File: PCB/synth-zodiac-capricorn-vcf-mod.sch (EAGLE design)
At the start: 35 parts, among them Q10 PNP, Q11 NPN, Q9 PNP, U11 TL074A, U12 LM13700

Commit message: Snapshot of designs so far.
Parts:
- removed C36, C39, C40: 0.1uF, rlc:CAPACITOR0603
- removed CP_GND, CP_LFO_CV: PADSMD-070X070, con-testpoints:PADSMD-070X070
- removed GLYPH1: Virgo, circuit-monkey-zodiac:GLYPH-VIRGO
- removed LED: BLU, led:SMT0603
- removed LFO_SQ, LFO_TRI: TPSMD-040-RND, con-testpoints:TPSMD-040-RND
- removed OUT_VCF, OUT_VCO: 2-pin, VT, SMT, con-jst:02PVT-SMT
- removed PWR: (no value), con-jst:04P-VT-SMT
- removed Q10, Q9: PNP, transistor-bjt:PNP-BC856
- removed Q11: NPN, transistor-bjt:NPN-BC846
- removed R58: 274K, rlc:RESISTOR0603
- removed R59: 3.32, rlc:RESISTOR0603
- removed R60: 221K, rlc:RESISTOR0603
- removed R61, R64: 499K, rlc:RESISTOR0603
- removed R62, R63, R68: 10.0K, rlc:RESISTOR0603
- removed R65: 47.5K, rlc:RESISTOR0603
- removed R66: 1.0K, rlc:RESISTOR0603
- removed R67: 22.1K, rlc:RESISTOR0603
- removed R69: 12.1K, rlc:RESISTOR0603
- removed RATE: 10K, rlc:TRIMPOT9MM_PCB_SHAFT
- removed U11: TL074A, op-amp:QUADTL074A-SOIC
- removed U12: LM13700, op-amp:DUAL-BIASLM13700-SMD
- removed WAVE: SPDT, switch-thd:SLIDE-SPDTSS-12-F45-TH-PCB
- added AMT: 10K, rlc:TRIMPOT9MM_PCB_SHAFT
- added EG, LFO, VCF_OUT: 2-pin, VT, SMT, con-jst:02PVT-SMT
- added J4: (no value), con-jst:04P-VT-SMT
- added POL, SRC: SPDT, switch-thd:SLIDE-SPDTSS-12-F45-TH-PCB
- added R72, R73: 10.0K, rlc:RESISTOR0603
- added U1: TL072A, op-amp:DUALTL072A
- CONST1: value Virgo -> Capricorn; device circuit-monkey-zodiac:CONSTELLATION-VIRGO -> circuit-monkey-zodiac:CONSTELLATION-CAPRICORN
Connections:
- removed net LFO_CV_IN: CP_LFO_CV.PAD, R60.1
- removed net LFO_OSC: R63.2, U11-D.+, U12-A.+, U12-B.+, U12-B.OUT
- removed net LFO_SQ: LFO_SQ.P$1, U11-D.-, U11-D.OUT, WAVE-SW.B
- removed net LFO_TRI: LFO_TRI.P$1, U11-A.-, U11-A.OUT, WAVE-SW.A
- removed net N$76: R58.1, RATE.2
- removed net N$77: Q9.BASE, R58.2, R59.1, R60.2
- removed net N$79: Q9.EMITTER, R61.2, U11-C.+
- removed net N$80: Q10.EMITTER, U11-C.-, U11-C.OUT
- removed net N$81: Q10.COLLECTOR, R62.1
- removed net N$82: R62.2, U12-A.AMP-BIAS
- removed net N$83: C36.1, U12-A-BUFFER.IN, U12-A.OUT
- removed net N$85: R64.1, U11-A.+, U12-A-BUFFER.OUT, U12-B.-
- removed net N$87: R65.1, U12-B.AMP-BIAS
- removed net N$88: Q11.BASE, R67.2, R68.2
- removed net N$89: Q11.EMITTER, R66.1
- removed net N$90: R68.1, R69.1, U12-B-BUFFER.OUT
- removed net N$91: LED.C, Q11.COLLECTOR
- new net AMT: AMT.2, U1-A.+
- new net EG: EG.1, SRC-SW.B
- new net MOD_N: POL-SW.A, R72.2, U1-B.OUT
- new net MOD_P: POL-SW.B, R73.1, U1-A.-, U1-A.OUT
- new net MOD_SRC: AMT.3, SRC-SW.C
- new net N$99: R72.1, R73.2, U1-B.-
- new net VCF_MOD: POL-SW.C, VCF_OUT.1
- net +9V: now also J4.1, U1-PWR.V+; no longer C39.1, LED.A, PWR.1, R61.1, R65.2, R67.1, RATE.3, U11-PWR.V+, U12-PWR.V+
- net -9V: now also J4.2, U1-PWR.V-; no longer C40.2, PWR.2, R64.2, R69.2, RATE.1, U11-PWR.V-, U12-PWR.V-
- net GND: now also AMT.1, EG.2, J4.4, LFO.2, POL-MTG.MT1, POL-MTG.MT2, SRC-MTG.MT1, SRC-MTG.MT2, U1-B.+, VCF_OUT.2; no longer C36.2, C39.2, C40.1, CP_GND.PAD, OUT_VCF.2, OUT_VCO.2, PWR.4, Q10.BASE, Q9.COLLECTOR, R59.2, R63.1, R66.2, U12-A.-
- net LFO_CV: now also LFO.1, SRC-SW.A; no longer OUT_VCF.1, OUT_VCO.1, U12-B-BUFFER.IN, WAVE-SW.C
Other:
- note added: "NC"
- note added: "POLARITY"
- note added: "VCF MODULATOR"
- note added: "VCF Modulation Amount"
- note added: "VCF Modulation Source"
- note added: "[+]"
- note added: "[-]"
- note removed: "==> VCF MOD"
- note removed: "==> VCO MOD"
- note removed: "CV_PNL ===>"
- note removed: "LFO"
- note removed: "LFO RATE"
- note removed: "LFO WAVE"
- note removed: "SQ"
- note removed: "TRI"
- moved on the sheet: C41, C42, CONST1, PCB1

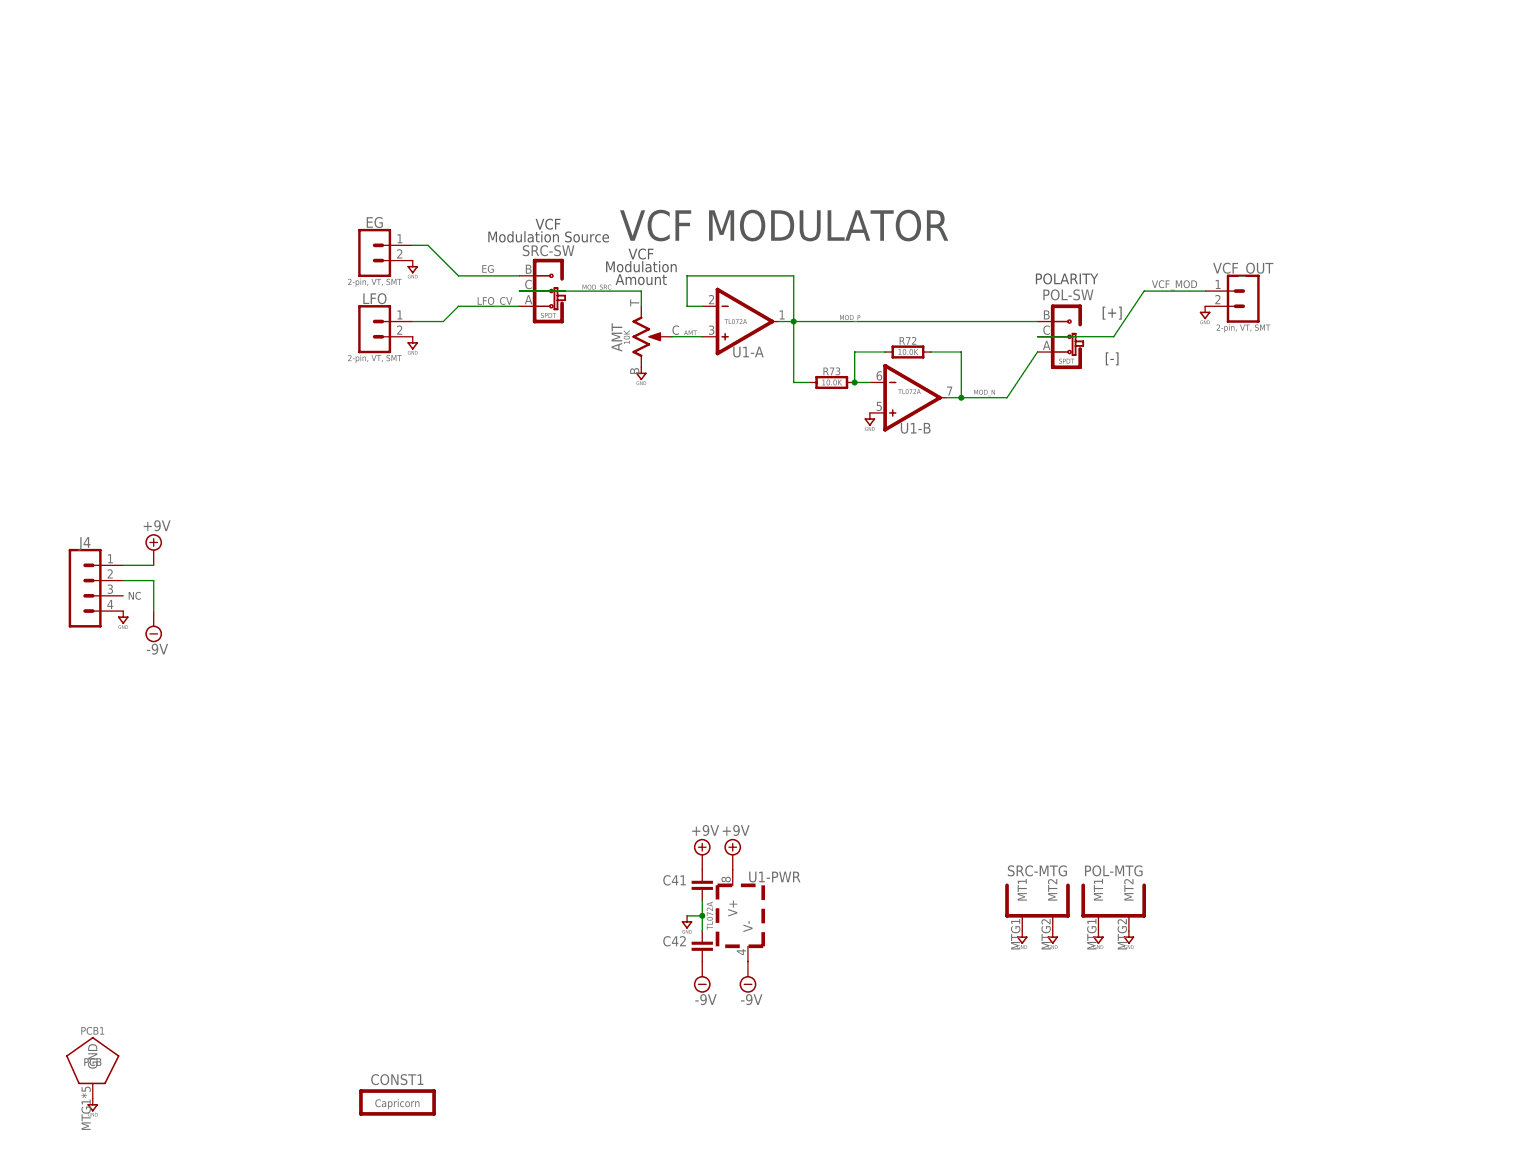
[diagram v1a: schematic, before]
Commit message: Almost ready for FAB.
Sagittarius was mis-spelled, renamed it.  Taurus is still WIP.
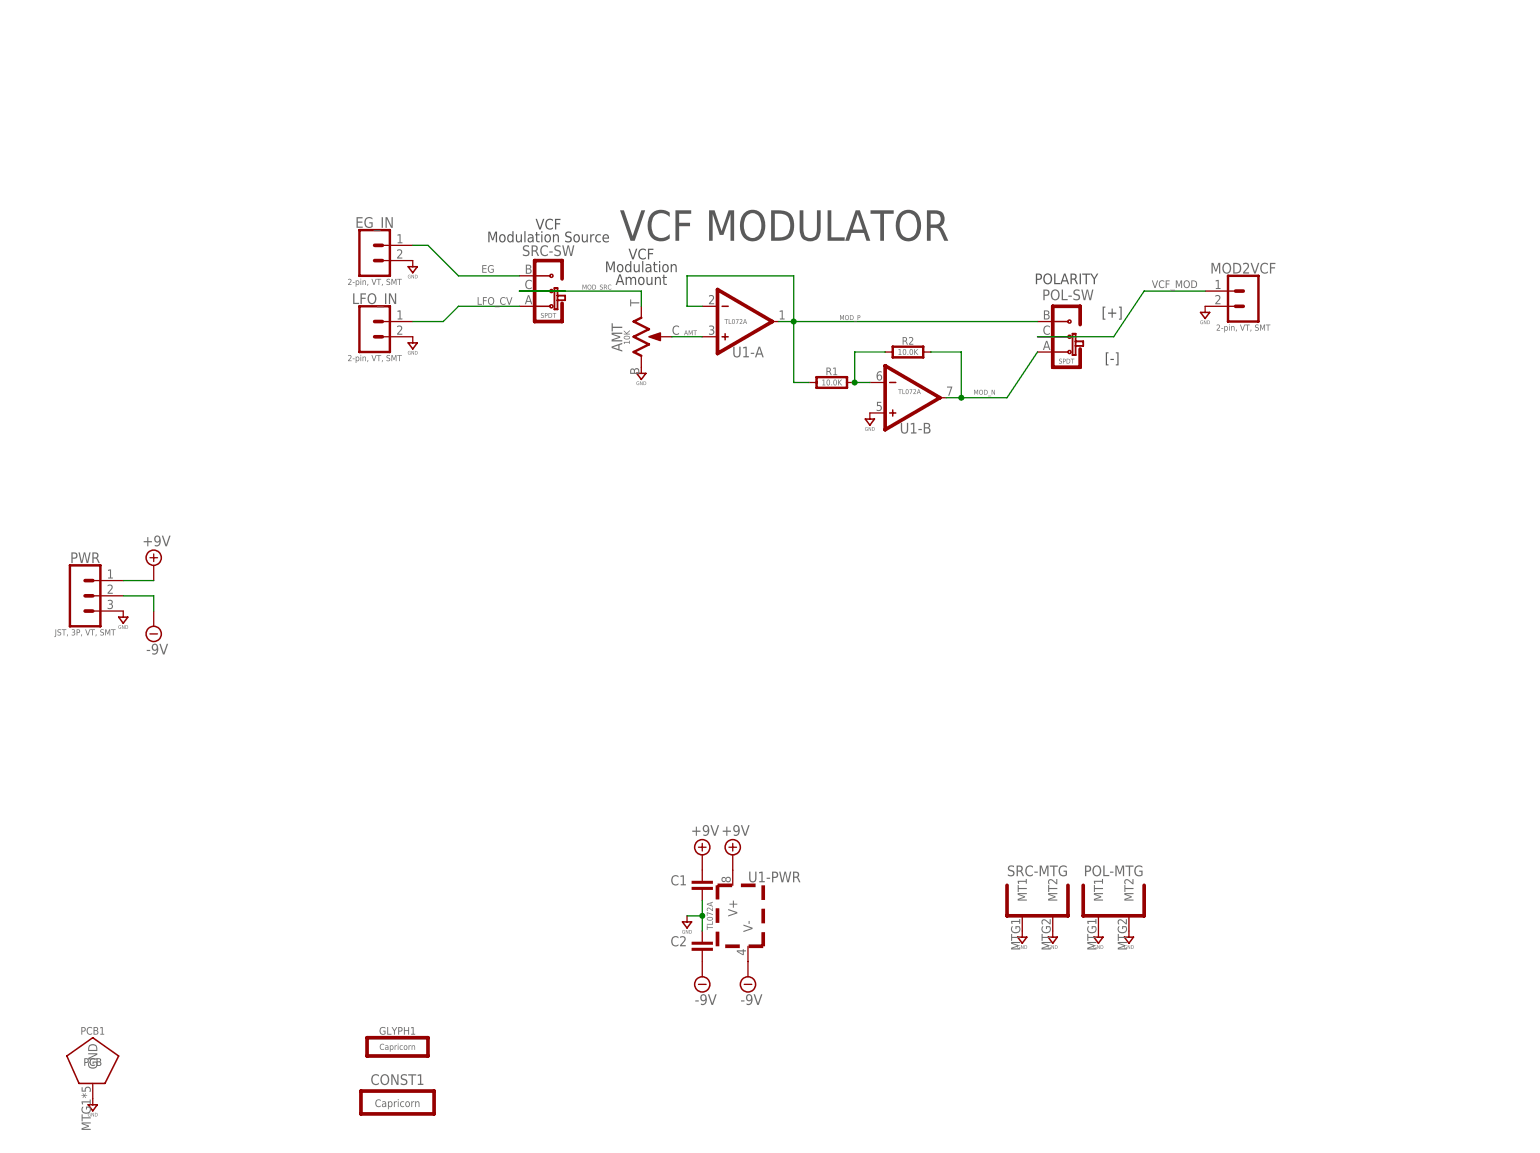
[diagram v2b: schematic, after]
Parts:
- removed J4: (no value), con-jst:04P-VT-SMT
- added GLYPH1: Capricorn, circuit-monkey-zodiac:GLYPH-CAPRICORN
- added PWR: JST, 3P, VT, SMT, con-jst:03P-VT-SMT
- renumbered C41 to C1, C42 to C2, EG to EG_IN, LFO to LFO_IN, R72 to R2, R73 to R1, VCF_OUT to MOD2VCF
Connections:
- net +9V: now also PWR.1; no longer J4.1
- net -9V: now also PWR.2; no longer J4.2
- net GND: now also PWR.3; no longer J4.4
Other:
- note removed: "NC"

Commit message: Work in progress for rev A,  VCO rev.B
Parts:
- EG_IN, LFO_IN, MOD2VCF: value 2-pin, VT, SMT -> JST, SH, 2P; device con-jst:02PVT-SMT -> con-jst:02P-SM-VT-SMT
- POL, SRC: value SPDT -> (none); device switch-thd:SLIDE-SPDTSS-12-F45-TH-PCB -> switch-thd:SLIDE-SPDT-MNTSS-12-F45-TH-PCB
- PWR: value JST, 3P, VT, SMT -> JST SM 3P; device con-jst:03P-VT-SMT -> con-jst:03P-SM-VT-SMT
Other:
- note added: "Capricorn"
- note added: "SATAN'S CYCLE WORKS"
- note added: "VCF Mod"
- note added: "Zodiac Synth"
- moved on the sheet: AMT, C1, C2, EG_IN, LFO_IN, MOD2VCF, PCB1, POL, POL-MTG, PWR, R1, R2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

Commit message: Perhaps final Rev. A?
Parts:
- POL, SRC: device switch-thd:SLIDE-SPDT-MNTSS-12-F45-TH-PCB -> switch-thd:SLIDE-SPDT-MNTSS-12-F45-TH-PCB-2
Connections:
- net EG: now also SRC-SW.A; no longer SRC-SW.B
- net LFO_CV: now also SRC-SW.B; no longer SRC-SW.A
- net MOD_N: now also POL-SW.B; no longer POL-SW.A
- net MOD_P: now also POL-SW.A; no longer POL-SW.B
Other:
- moved on the sheet: POL-MTG, POL-SW, SRC-MTG, SRC-SW
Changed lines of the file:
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@@
 <part name="R1" library="rlc" library_urn="urn:adsk.eagle:library:4192893" deviceset="RESISTOR" device="0603" package3d_urn="urn:adsk.eagle:package:4193040/5" value="10.0K"/>
 <part name="SUPPLY90" library="supply" library_urn="urn:adsk.eagle:library:10485988" deviceset="GND" device=""/>
-<part name="C1" library="rlc" library_urn="urn:adsk.eagle:library:4192893" deviceset="CAPACITOR" device="0603" package3d_urn="urn:adsk.eagle:package:4193021/4" value="0.1uF"/>
-<part name="C2" library="rlc" library_urn="urn:adsk.eagle:library:4192893" deviceset="CAPACITOR" device="0603" package3d_urn="urn:adsk.eagle:package:4193021/4" value="0.1uF"/>
+<part name="C1" library="rlc" library_urn="urn:adsk.eagle:library:4192893" deviceset="CAPACITOR" device="0603" package3d_urn="urn:adsk.eagle:package:4193021/5" value="0.1uF"/>
+<part name="C2" library="rlc" library_urn="urn:adsk.eagle:library:4192893" deviceset="CAPACITOR" device="0603" package3d_urn="urn:adsk.eagle:package:4193021/5" value="0.1uF"/>
 <part name="SUPPLY95" library="supply" library_urn="urn:adsk.eagle:library:10485988" deviceset="GND" device=""/>
 <part name="SUPPLY101" library="supply" library_urn="urn:adsk.eagle:library:10485988" deviceset="-9V" device=""/>
@@
 <part name="SUPPLY3" library="supply" library_urn="urn:adsk.eagle:library:10485988" deviceset="-9V" device=""/>
 <part name="SUPPLY4" library="supply" library_urn="urn:adsk.eagle:library:10485988" deviceset="GND" device=""/>
-<part name="AMT" library="rlc" library_urn="urn:adsk.eagle:library:4192893" deviceset="TRIMPOT" device="9MM_PCB_SHAFT" package3d_urn="urn:adsk.eagle:package:36472483/2" value="10K"/>
+<part name="AMT" library="rlc" library_urn="urn:adsk.eagle:library:4192893" deviceset="TRIMPOT" device="9MM_PCB_SHAFT" package3d_urn="urn:adsk.eagle:package:36472483/3" value="10K"/>
 <part name="U1" library="op-amp" library_urn="urn:adsk.eagle:library:7076615" deviceset="DUAL" device="TL072A" package3d_urn="urn:adsk.eagle:package:8032603/4" value="TL072A"/>
 <part name="SUPPLY5" library="supply" library_urn="urn:adsk.eagle:library:10485988" deviceset="GND" device=""/>
@@
 <part name="LFO_IN" library="con-jst" library_urn="urn:adsk.eagle:library:7191852" deviceset="02P" device="-SM-VT-SMT" package3d_urn="urn:adsk.eagle:package:41368283/6" value="JST, SH, 2P"/>
 <part name="MOD2VCF" library="con-jst" library_urn="urn:adsk.eagle:library:7191852" deviceset="02P" device="-SM-VT-SMT" package3d_urn="urn:adsk.eagle:package:41368283/6" value="JST, SH, 2P"/>
-<part name="SRC" library="switch-thd" library_urn="urn:adsk.eagle:library:26242324" deviceset="SLIDE-SPDT-MNT" device="SS-12-F45-TH-PCB" package3d_urn="urn:adsk.eagle:package:36475164/3"/>
-<part name="POL" library="switch-thd" library_urn="urn:adsk.eagle:library:26242324" deviceset="SLIDE-SPDT-MNT" device="SS-12-F45-TH-PCB" package3d_urn="urn:adsk.eagle:package:36475164/3"/>
+<part name="SRC" library="switch-thd" library_urn="urn:adsk.eagle:library:26242324" deviceset="SLIDE-SPDT-MNT" device="SS-12-F45-TH-PCB-2"/>
+<part name="POL" library="switch-thd" library_urn="urn:adsk.eagle:library:26242324" deviceset="SLIDE-SPDT-MNT" device="SS-12-F45-TH-PCB-2"/>
 </parts>
 <sheets>
@@
 <attribute name="NAME" x="194.31" y="95.25" size="1.778" layer="95" font="vector" ratio="15" rot="MR0" align="center"/>
 </instance>
-<instance part="SRC" gate="-SW" x="76.2" y="99.06" smashed="yes" rot="MR90">
-<attribute name="NAME" x="76.2" y="105.664" size="1.778" layer="95" ratio="15" rot="MR0" align="center"/>
-<attribute name="VALUE" x="81.788" y="99.314" size="0.8128" layer="96" rot="MR90" align="center"/>
-</instance>
-<instance part="POL" gate="-SW" x="162.56" y="91.44" smashed="yes" rot="MR90">
-<attribute name="NAME" x="162.56" y="98.044" size="1.778" layer="95" ratio="15" rot="MR0" align="center"/>
-<attribute name="VALUE" x="168.148" y="91.694" size="0.8128" layer="96" rot="MR90" align="center"/>
+<instance part="SRC" gate="-SW" x="76.2" y="99.06" smashed="yes" rot="R270">
+<attribute name="NAME" x="76.2" y="92.456" size="1.778" layer="95" ratio="15" rot="R180" align="center"/>
+<attribute name="VALUE" x="81.788" y="98.806" size="0.8128" layer="96" rot="R270" align="center"/>
+</instance>
+<instance part="POL" gate="-SW" x="162.56" y="91.44" smashed="yes" rot="R270">
+<attribute name="NAME" x="162.56" y="84.836" size="1.778" layer="95" ratio="15" rot="R180" align="center"/>
+<attribute name="VALUE" x="168.148" y="91.186" size="0.8128" layer="96" rot="R270" align="center"/>
 </instance>
 <instance part="SRC" gate="-MTG" x="220.98" y="27.94" smashed="yes">
@@
 <pinref part="LFO_IN" gate="G$1" pin="1"/>
 <wire x1="53.34" y1="93.98" x2="48.26" y2="93.98" width="0.1524" layer="91"/>
-<pinref part="SRC" gate="-SW" pin="A"/>
+<pinref part="SRC" gate="-SW" pin="B"/>
 </segment>
 </net>
@@
 <pinref part="U1" gate="-A" pin="-"/>
 <pinref part="U1" gate="-A" pin="OUT"/>
-<pinref part="POL" gate="-SW" pin="B"/>
+<pinref part="POL" gate="-SW" pin="A"/>
 </segment>
 </net>
@@
 <segment>
 <wire x1="91.44" y1="96.52" x2="91.44" y2="99.06" width="0.1524" layer="91"/>
-<wire x1="91.44" y1="99.06" x2="78.74" y2="99.06" width="0.1524" layer="91"/>
-<wire x1="71.12" y1="99.06" x2="78.74" y2="99.06" width="0.1524" layer="91"/>
+<wire x1="91.44" y1="99.06" x2="71.12" y2="99.06" width="0.1524" layer="91"/>
 <label x="81.534" y="99.314" size="0.8128" layer="95"/>
 <pinref part="AMT" gate="G$1" pin="3"/>
@@
 <pinref part="EG_IN" gate="G$1" pin="1"/>
 <wire x1="53.34" y1="106.68" x2="48.26" y2="106.68" width="0.1524" layer="91"/>
-<pinref part="SRC" gate="-SW" pin="B"/>
+<pinref part="SRC" gate="-SW" pin="A"/>
 </segment>
 </net>
@@
 <wire x1="144.78" y1="88.9" x2="144.78" y2="81.28" width="0.1524" layer="91"/>
 <junction x="144.78" y="81.28"/>
-<wire x1="157.48" y1="88.9" x2="152.4" y2="81.28" width="0.1524" layer="91"/>
 <wire x1="152.4" y1="81.28" x2="144.78" y2="81.28" width="0.1524" layer="91"/>
 <label x="146.812" y="81.788" size="0.8128" layer="95"/>
 <pinref part="U1" gate="-B" pin="OUT"/>
-<pinref part="POL" gate="-SW" pin="A"/>
-</segment>
-</net>
+<pinref part="POL" gate="-SW" pin="B"/>
+<wire x1="152.4" y1="81.28" x2="157.48" y2="88.9" width="0.1524" layer="91"/>
+</segment>
+</net>
